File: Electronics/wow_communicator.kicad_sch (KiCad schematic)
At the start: 0 parts

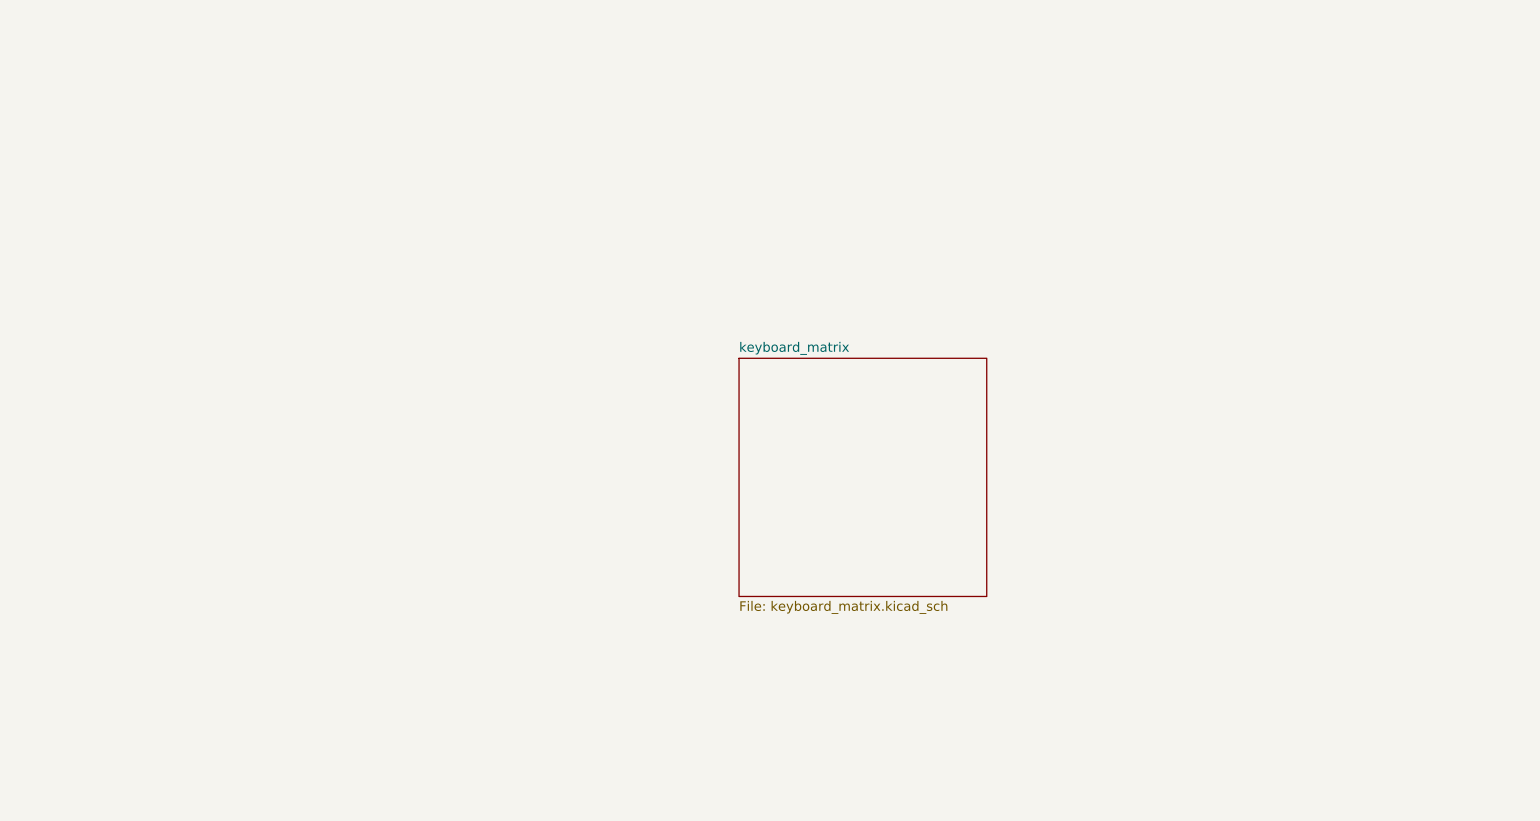
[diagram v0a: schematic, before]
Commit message: arranged keys for keyboard. marked out lcd
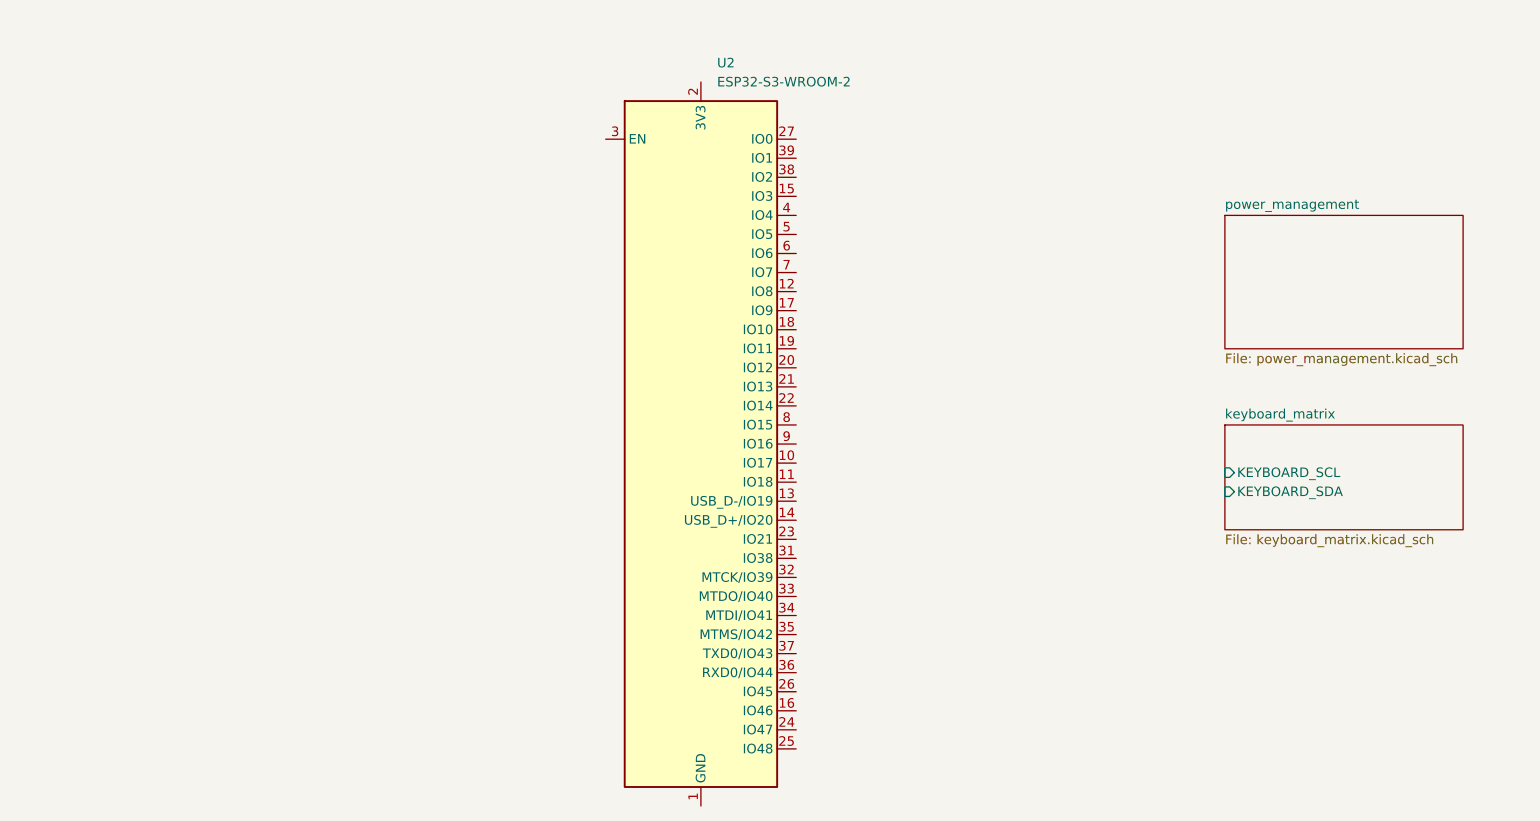
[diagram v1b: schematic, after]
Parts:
- added U2: ESP32-S3-WROOM-2, RF_Module:ESP32-S3-WROOM-2, symbol RF_Module:ESP32-S3-WROOM-2
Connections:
- new net: U2.1 (GND), U2.40 (GND), U2.41 (GND)
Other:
- added sheet power_management (power_management.kicad_sch)
- sheet keyboard_matrix ports: added KEYBOARD_SCL, KEYBOARD_SDA; removed none
- company: (none) -> WebWow
- title: (none) -> WebWow Communicator
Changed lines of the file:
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@@
 	(generator_version "9.0")
 	(paper "A4")
+	(title_block
+		(title "WebWow Communicator")
+		(date "2025-07-20")
+		(rev "A0")
+		(company "WebWow")
+		(comment 1 "Bjorn Hropot")
+	)
+	(symbol
+		(lib_id "RF_Module:ESP32-S3-WROOM-2")
+		(at 143.51 97.79 0)
+		(unit 1)
+		(exclude_from_sim no)
+		(in_bom yes)
+		(on_board yes)
+		(dnp no)
+		(fields_autoplaced yes)
+		(property "Reference" "U2"
+			(at 145.6533 46.99 0)
+			(effects
+				(font
+					(size 1.27 1.27)
+				)
+				(justify left)
+			)
+		)
+		(property "Value" "ESP32-S3-WROOM-2"
+			(at 145.6533 49.53 0)
+			(effects
+				(font
+					(size 1.27 1.27)
+				)
+				(justify left)
+			)
+		)
+		(property "Footprint" "RF_Module:ESP32-S3-WROOM-2"
+			(at 143.51 158.75 0)
+			(effects
+				(font
+					(size 1.27 1.27)
+				)
+				(hide yes)
+			)
+		)
+		(property "Datasheet" "https://www.espressif.com/sites/default/files/documentation/esp32-s3-wroom-2_datasheet_en.pdf"
+			(at 143.51 161.29 0)
+			(effects
+				(font
+					(size 1.27 1.27)
+				)
+				(hide yes)
+			)
+		)
+		(property "Description" "RF Module, 2.4 GHz, Wi­-Fi, Bluetooth, BLE, ESP32­-S3R8V"
+			(at 143.51 97.79 0)
+			(effects
+				(font
+					(size 1.27 1.27)
+				)
+				(hide yes)
+			)
+		)
+		(pin "26"
+		)
+		(pin "18"
+		)
+		(pin "13"
+		)
+		(pin "16"
+		)
+		(pin "34"
+		)
+		(pin "24"
+		)
+		(pin "36"
+		)
+		(pin "35"
+		)
+		(pin "12"
+		)
+		(pin "37"
+		)
+		(pin "25"
+		)
+		(pin "14"
+		)
+		(pin "6"
+		)
+		(pin "27"
+		)
+		(pin "29"
+		)
+		(pin "41"
+		)
+		(pin "38"
+		)
+		(pin "3"
+		)
+		(pin "30"
+		)
+		(pin "33"
+		)
+		(pin "20"
+		)
+		(pin "8"
+		)
+		(pin "10"
+		)
+		(pin "21"
+		)
+		(pin "23"
+		)
+		(pin "22"
+		)
+		(pin "4"
+		)
+		(pin "5"
+		)
+		(pin "11"
+		)
+		(pin "17"
+		)
+		(pin "7"
+		)
+		(pin "28"
+		)
+		(pin "32"
+		)
+		(pin "2"
+		)
+		(pin "9"
+		)
+		(pin "40"
+		)
+		(pin "1"
+		)
+		(pin "31"
+		)
+		(pin "19"
+		)
+		(pin "15"
+		)
+		(pin "39"
+		)
+		(instances
+			(project ""
+				(path "/99202413-db31-4104-a376-6ecb768b1972"
+					(reference "U2")
+					(unit 1)
+				)
+			)
+		)
+	)
 	(sheet
-		(at 148.59 86.36)
-		(size 33.02 31.75)
+		(at 213.36 67.31)
+		(size 31.75 17.78)
 		(exclude_from_sim no)
 		(in_bom yes)
@@
 			(color 0 0 0 0.0000)
 		)
+		(property "Sheetname" "power_management"
+			(at 213.36 66.5984 0)
+			(effects
+				(font
+					(size 1.27 1.27)
+				)
+				(justify left bottom)
+			)
+		)
+		(property "Sheetfile" "power_management.kicad_sch"
+			(at 213.36 85.6746 0)
+			(effects
+				(font
+					(size 1.27 1.27)
+				)
+				(justify left top)
+			)
+		)
+		(instances
+			(project "wow_communicator"
+				(path "/99202413-db31-4104-a376-6ecb768b1972"
+					(page "3")
+				)
+			)
+		)
+	)
+	(sheet
+		(at 213.36 95.25)
+		(size 31.75 13.97)
+		(exclude_from_sim no)
+		(in_bom yes)
+		(on_board yes)
+		(dnp no)
+		(fields_autoplaced yes)
+		(stroke
+			(width 0.1524)
+			(type solid)
+		)
+		(fill
+			(color 0 0 0 0.0000)
+		)
 		(property "Sheetname" "keyboard_matrix"
-			(at 148.59 85.6484 0)
+			(at 213.36 94.5384 0)
 			(effects
 				(font
@@
 		)
 		(property "Sheetfile" "keyboard_matrix.kicad_sch"
-			(at 148.59 118.6946 0)
+			(at 213.36 109.8046 0)
 			(effects
 				(font
@@
 			)
 		)
+		(pin "KEYBOARD_SCL" input
+			(at 213.36 101.6 180)
+			(effects
+				(font
+					(size 1.27 1.27)
+				)
+				(justify left)
+			)
+		)
+		(pin "KEYBOARD_SDA" input
+			(at 213.36 104.14 180)
+			(effects
+				(font
+					(size 1.27 1.27)
+				)
+				(justify left)
+			)
+		)

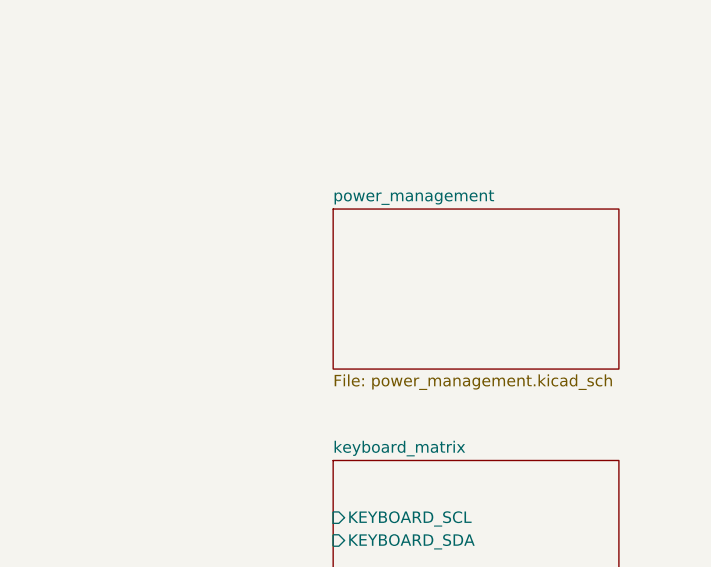
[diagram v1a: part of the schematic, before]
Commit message: basic power supply layout some minor design notes. charge ic likely to change. possibly bridge out fuel gague
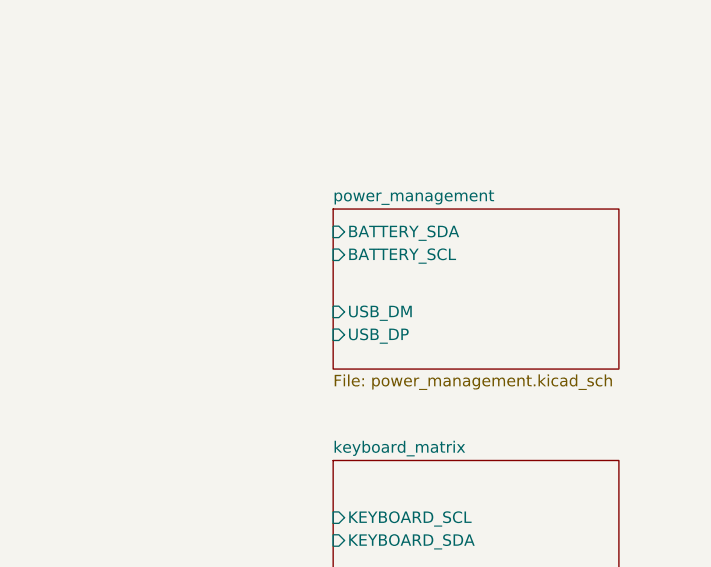
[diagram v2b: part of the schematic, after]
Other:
- sheet power_management ports: added BATTERY_SCL, BATTERY_SDA, USB_DM, USB_DP; removed none
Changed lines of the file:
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@@
+			)
+		)
+		(pin "USB_DP" input
+			(at 213.36 81.28 180)
+			(effects
+				(font
+					(size 1.27 1.27)
+				)
+				(justify left)
+			)
+		)
+		(pin "USB_DM" input
+			(at 213.36 78.74 180)
+			(effects
+				(font
+					(size 1.27 1.27)
+				)
+				(justify left)
+			)
+		)
+		(pin "BATTERY_SDA" input
+			(at 213.36 69.85 180)
+			(effects
+				(font
+					(size 1.27 1.27)
+				)
+				(justify left)
+			)
+		)
+		(pin "BATTERY_SCL" input
+			(at 213.36 72.39 180)
+			(effects
+				(font
+					(size 1.27 1.27)
+				)
+				(justify left)
 			)
 		)

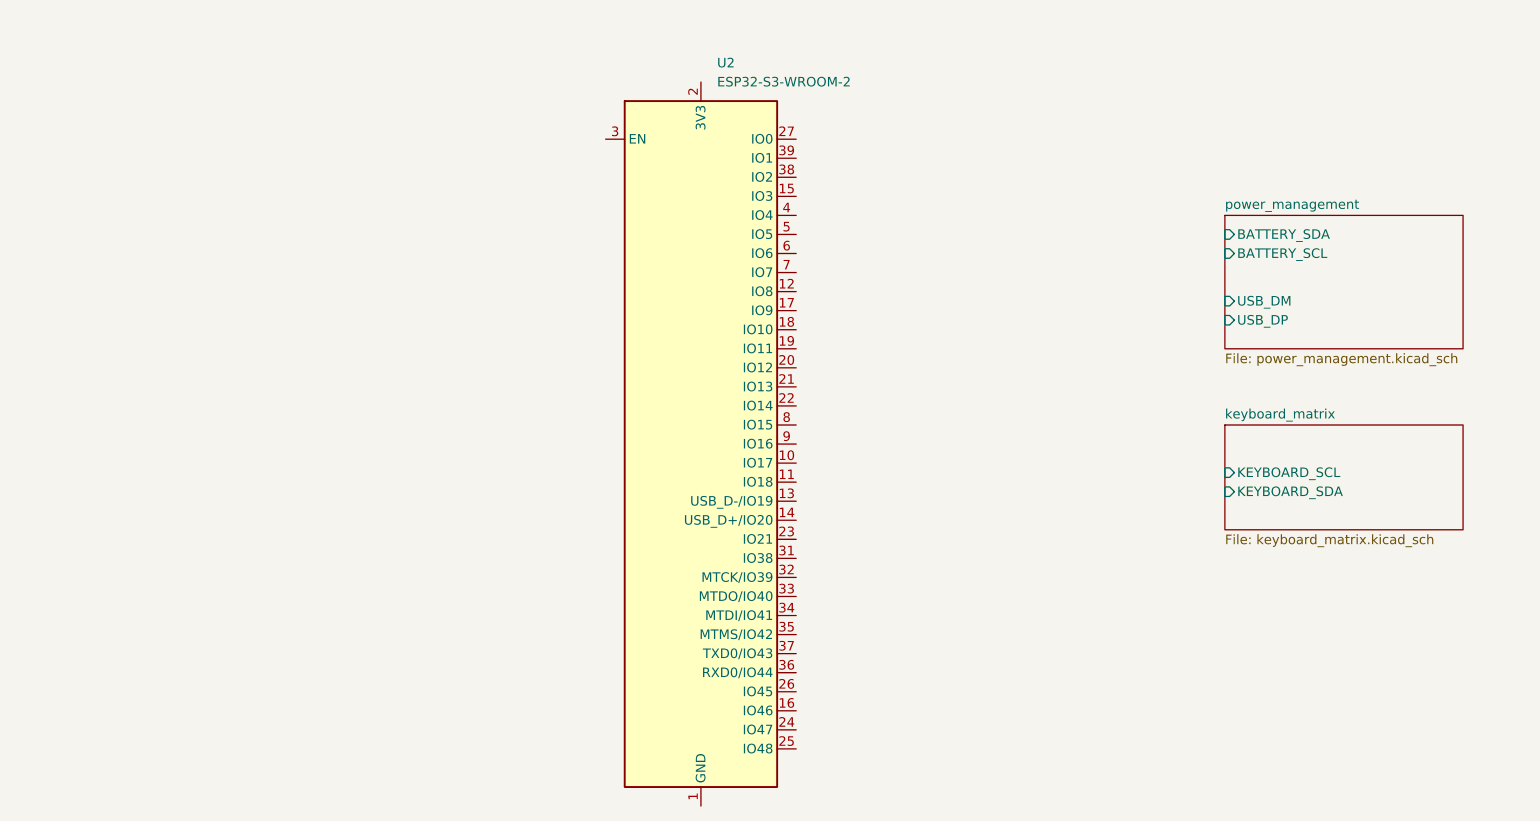
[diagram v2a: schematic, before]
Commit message: created LCD library started pinout
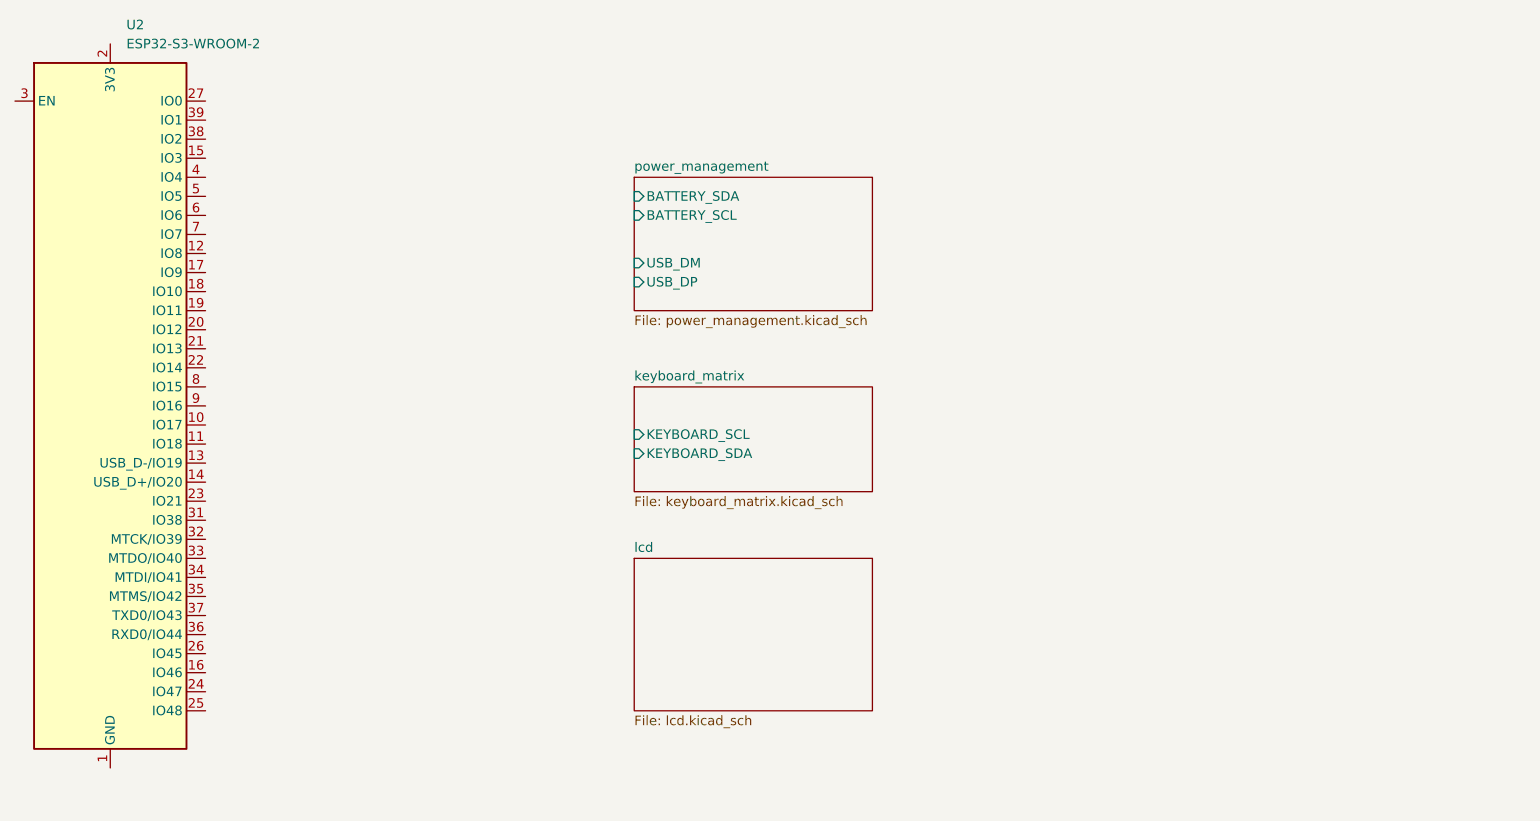
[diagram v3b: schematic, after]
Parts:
- U2: Manufacturer (none) -> Espressif; Part Number (none) -> ESP32-S3-WROOM-2
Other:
- added sheet lcd (lcd.kicad_sch)
- moved on the sheet: U2
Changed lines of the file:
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@@
 	(symbol
 		(lib_id "RF_Module:ESP32-S3-WROOM-2")
-		(at 143.51 97.79 0)
+		(at 64.77 92.71 0)
 		(unit 1)
 		(exclude_from_sim no)
@@
 		(fields_autoplaced yes)
 		(property "Reference" "U2"
-			(at 145.6533 46.99 0)
+			(at 66.9133 41.91 0)
 			(effects
 				(font
@@
 		)
 		(property "Value" "ESP32-S3-WROOM-2"
-			(at 145.6533 49.53 0)
+			(at 66.9133 44.45 0)
 			(effects
 				(font
@@
 		)
 		(property "Footprint" "RF_Module:ESP32-S3-WROOM-2"
-			(at 143.51 158.75 0)
-			(effects
-				(font
-					(size 1.27 1.27)
-				)
-				(hide yes)
-			)
-		)
-		(property "Datasheet" "https://www.espressif.com/sites/default/files/documentation/esp32-s3-wroom-2_datasheet_en.pdf"
-			(at 143.51 161.29 0)
+			(at 64.77 153.67 0)
+			(effects
+				(font
+					(size 1.27 1.27)
+				)
+				(hide yes)
+			)
+		)
+		(property "Datasheet" "datsheet/esp32-s3-wroom-2_datasheet_en.pdf"
+			(at 64.77 156.21 0)
 			(effects
 				(font
@@
 		)
 		(property "Description" "RF Module, 2.4 GHz, Wi­-Fi, Bluetooth, BLE, ESP32­-S3R8V"
-			(at 143.51 97.79 0)
+			(at 64.77 92.71 0)
+			(effects
+				(font
+					(size 1.27 1.27)
+				)
+				(hide yes)
+			)
+		)
+		(property "Manufacturer" "Espressif"
+			(at 64.77 92.71 0)
+			(effects
+				(font
+					(size 1.27 1.27)
+				)
+				(hide yes)
+			)
+		)
+		(property "Part Number" "ESP32-S3-WROOM-2"
+			(at 64.77 92.71 0)
 			(effects
 				(font
@@
 	)
 	(sheet
-		(at 213.36 67.31)
+		(at 134.62 113.03)
+		(size 31.75 20.32)
+		(exclude_from_sim no)
+		(in_bom yes)
+		(on_board yes)
+		(dnp no)
+		(fields_autoplaced yes)
+		(stroke
+			(width 0.1524)
+			(type solid)
+		)
+		(fill
+			(color 0 0 0 0.0000)
+		)
+		(property "Sheetname" "lcd"
+			(at 134.62 112.3184 0)
+			(effects
+				(font
+					(size 1.27 1.27)
+				)
+				(justify left bottom)
+			)
+		)
+		(property "Sheetfile" "lcd.kicad_sch"
+			(at 134.62 133.9346 0)
+			(effects
+				(font
+					(size 1.27 1.27)
+				)
+				(justify left top)
+			)
+		)
+		(instances
+			(project "wow_communicator"
+				(path "/99202413-db31-4104-a376-6ecb768b1972"
+					(page "4")
+				)
+			)
+		)
+	)
+	(sheet
+		(at 134.62 62.23)
 		(size 31.75 17.78)
 		(exclude_from_sim no)
@@
 		)
 		(property "Sheetname" "power_management"
-			(at 213.36 66.5984 0)
+			(at 134.62 61.5184 0)
 			(effects
 				(font
@@
 		)
 		(property "Sheetfile" "power_management.kicad_sch"
-			(at 213.36 85.6746 0)
+			(at 134.62 80.5946 0)
 			(effects
 				(font
@@
 		)
 		(pin "USB_DP" input
-			(at 213.36 81.28 180)
+			(at 134.62 76.2 180)
 			(effects
 				(font
@@
 		)
 		(pin "USB_DM" input
-			(at 213.36 78.74 180)
+			(at 134.62 73.66 180)
 			(effects
 				(font
@@
 		)
 		(pin "BATTERY_SDA" input
-			(at 213.36 69.85 180)
+			(at 134.62 64.77 180)
 			(effects
 				(font
@@
 		)
 		(pin "BATTERY_SCL" input
-			(at 213.36 72.39 180)
+			(at 134.62 67.31 180)
 			(effects
 				(font
@@
 	)
 	(sheet
-		(at 213.36 95.25)
+		(at 134.62 90.17)
 		(size 31.75 13.97)
 		(exclude_from_sim no)
@@
 		)
 		(property "Sheetname" "keyboard_matrix"
-			(at 213.36 94.5384 0)
+			(at 134.62 89.4584 0)
 			(effects
 				(font
@@
 		)
 		(property "Sheetfile" "keyboard_matrix.kicad_sch"
-			(at 213.36 109.8046 0)
+			(at 134.62 104.7246 0)
 			(effects
 				(font
@@
 		)
 		(pin "KEYBOARD_SCL" input
-			(at 213.36 101.6 180)
+			(at 134.62 96.52 180)
 			(effects
 				(font
@@
 		)
 		(pin "KEYBOARD_SDA" input
-			(at 213.36 104.14 180)
-			(effects
-				(font
+			(at 134.62 99.06 180)
+			(effects
+				(font
